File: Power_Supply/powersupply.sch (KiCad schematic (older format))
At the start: 70 parts, among them J101 USB_B_Micro, J2 1x2, J3 1x2, Q1 Q_PMOS_GDS, SW1 KMR2, SW2 joystick-K1-1506DN-01, U1 B0505S-2WR2, U101 AZ1117E-3.3, U102 INA199, U103 ATSAMD10D13A-SS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

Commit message: power supply changes
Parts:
- removed D101: 6V, Diode_SMD:D_SOD-123, symbol Device:D_Zener_Small
- removed R103: 4.99k, Resistor_SMD:R_0805_2012Metric, symbol Device:R_Small_US
- removed U1: B0505S-2WR2, powersupply:B0505S-2WR2-Isolator, symbol powersupply:RFM-0505S
- removed U103: ATSAMD10D13A-SS, Package_SO:SOIC-20W_7.5x12.8mm_P1.27mm, symbol powersupply:ATSAMD10D13A-SS
- added C106: 15uF, Capacitor_SMD:C_0805_2012Metric, symbol Device:C_Small
- added C107: .1 uF, Capacitor_SMD:C_0805_2012Metric, symbol Device:C_Small
- added C108, C109: 15pF, Capacitor_SMD:C_0805_2012Metric, symbol Device:C_Small
- added C110, C111, C112, C113: .1uF, Capacitor_SMD:C_0805_2012Metric, symbol Device:C_Small
- added C114: 1uF, Capacitor_SMD:C_0805_2012Metric, symbol Device:C_Small
- added C115: 10uF, Capacitor_SMD:C_0805_2012Metric, symbol Device:C_Small
- added FB101: ind, Capacitor_SMD:C_0805_2012Metric, symbol Device:Ferrite_Bead_Small
- added R121: 10k, Resistor_SMD:R_0805_2012Metric, symbol Device:R_Small_US
- added Y101: 8MHz, Crystal:Crystal_SMD_5032-2Pin_5.0x3.2mm, symbol Device:Crystal_Small
- Q1: value Q_PMOS_GDS -> IRF9Z24NPBF
- R101: value 150 -> 1k; footprint Resistor_SMD:R_1206_3216Metric -> Resistor_SMD:R_0805_2012Metric
- R111: value 4.99k -> 3.6k
- R116: value 2.32k -> 5.76k
- R120: renamed from R?; value 4.99k -> 1.5k
- R122: renamed from R1; footprint Resistor_THT:R_Axial_DIN0411_L9.9mm_D3.6mm_P12.70mm_Horizontal -> Resistor_SMD:R_0805_2012Metric
- R2: value 580 -> 4.99k
- U103: renamed from U?; value STM32F103C8Tx -> STM32F103C8T6; symbol MCU_ST_STM32F1:STM32F103C8Tx -> powersupply-rescue:STM32F103C8Tx-MCU_ST_STM32F1
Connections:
- net labels removed: SCL, SWCLK, SWDIO
- wire segments 101 -> 129
- no-connect marks 5 -> 17
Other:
- note removed: "2W Isolator"
- moved on the sheet: C103, C104, R104, R105, R111, R112, R120, SW1

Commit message: pin headers
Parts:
- added J4: Conn_01x03_Male, Connector:FanPinHeader_1x03_P2.54mm_Vertical, symbol Connector:Conn_01x03_Male
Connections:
- net GND: now also J4.2 (Pin_2)
- net SWDIO: now reaches U103.34 (PA13)
- net SWDIO: now also J4.1 (Pin_1)
- net SWCLK: now reaches U103.37 (PA14)
- net SWCLK: now also J4.3 (Pin_3)
- no-connect marks 17 -> 15
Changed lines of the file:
@@
 EESchema Schematic File Version 4
 LIBS:powersupply-cache
-EELAYER 29 0
+EELAYER 30 0
 EELAYER END
 $Descr A4 11693 8268
@@
 NoConn ~ 2150 4800
 NoConn ~ 2150 4900
-NoConn ~ 2150 5200
-NoConn ~ 2150 5300
 NoConn ~ 2150 5400
 Wire Notes Line
@@
 $EndComp
 Connection ~ 1050 1650
+$Comp
+L Connector:Conn_01x03_Male J4
+U 1 1 5D9C1B22
+P 2700 5650
+F 0 "J4" H 2808 5931 50  0000 C CNN
+F 1 "Conn_01x03_Male" H 2808 5840 50  0000 C CNN
+F 2 "Connector:FanPinHeader_1x03_P2.54mm_Vertical" H 2700 5650 50  0001 C CNN
+F 3 "~" H 2700 5650 50  0001 C CNN
+	1    2700 5650
+	1    0    0    -1
+$EndComp
+$Comp
+L power:GND #PWR0140
+U 1 1 5D9C2B47
+P 3350 5650
+F 0 "#PWR0140" H 3350 5400 50  0001 C CNN
+F 1 "GND" H 3355 5477 50  0000 C CNN
+F 2 "" H 3350 5650 50  0001 C CNN
+F 3 "" H 3350 5650 50  0001 C CNN
+	1    3350 5650
+	1    0    0    -1
+$EndComp
+Wire Wire Line
+	2900 5650 3350 5650
+Text Label 2900 5550 0    50   ~ 0
+SWDIO
+Text Label 2900 5750 0    50   ~ 0
+SWCLK
+Text Label 2150 5200 0    50   ~ 0
+SWDIO
+Text Label 2150 5300 0    50   ~ 0
+SWCLK
 $EndSCHEMATC

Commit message: save problems
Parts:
- J4: footprint Connector:FanPinHeader_1x03_P2.54mm_Vertical -> Connector_PinSocket_2.54mm:PinSocket_1x03_P2.54mm_Vertical
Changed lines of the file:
@@
 F 0 "J4" H 2808 5931 50  0000 C CNN
 F 1 "Conn_01x03_Male" H 2808 5840 50  0000 C CNN
-F 2 "Connector:FanPinHeader_1x03_P2.54mm_Vertical" H 2700 5650 50  0001 C CNN
+F 2 "Connector_PinSocket_2.54mm:PinSocket_1x03_P2.54mm_Vertical" H 2700 5650 50  0001 C CNN
 F 3 "~" H 2700 5650 50  0001 C CNN
 	1    2700 5650

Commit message: layout changes
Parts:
- D102: renamed from D1; footprint LED_THT:LED_D3.0mm -> LED_SMD:LED_0603_1608Metric_Pad1.05x0.95mm_HandSolder
- R123: renamed from R2; footprint Resistor_THT:R_Axial_DIN0207_L6.3mm_D2.5mm_P10.16mm_Horizontal -> Resistor_SMD:R_0805_2012Metric
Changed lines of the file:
@@
 EESchema Schematic File Version 4
 LIBS:powersupply-cache
-EELAYER 30 0
+EELAYER 29 0
 EELAYER END
 $Descr A4 11693 8268
@@
 	10850 4950 10850 5300
 $Comp
-L Device:LED D1
+L Device:LED D102
 U 1 1 5D62BB53
 P 3950 1300
-F 0 "D1" V 3989 1182 50  0000 R CNN
+F 0 "D102" V 3989 1182 50  0000 R CNN
 F 1 "C503B 2.1V" V 3898 1182 50  0000 R CNN
-F 2 "LED_THT:LED_D3.0mm" H 3950 1300 50  0001 C CNN
+F 2 "LED_SMD:LED_0603_1608Metric_Pad1.05x0.95mm_HandSolder" H 3950 1300 50  0001 C CNN
 F 3 "~" H 3950 1300 50  0001 C CNN
 	1    3950 1300
@@
 	9700 4250 9900 4250
 $Comp
-L Device:R_Small_US R2
+L Device:R_Small_US R123
 U 1 1 5D62CB9E
 P 3950 1050
-F 0 "R2" H 4018 1096 50  0000 L CNN
+F 0 "R123" H 4018 1096 50  0000 L CNN
 F 1 "4.99k" H 4018 1005 50  0000 L CNN
-F 2 "Resistor_THT:R_Axial_DIN0207_L6.3mm_D2.5mm_P10.16mm_Horizontal" H 3950 1050 50  0001 C CNN
+F 2 "Resistor_SMD:R_0805_2012Metric" H 3950 1050 50  0001 C CNN
 F 3 "~" H 3950 1050 50  0001 C CNN
 	1    3950 1050

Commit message: layout
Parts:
- removed TP10: pad_2, powersupply:pads, symbol Connector:TestPoint
- removed TP12: Pad1_default, powersupply:pads, symbol Connector:TestPoint
- removed TP13: pin_2_pad_alt, powersupply:pads, symbol Connector:TestPoint
- removed TP9: pad_1, powersupply:pads, symbol Connector:TestPoint
- added J103, J104: Default_Jumper, powersupply:Default_Jumper, symbol powersupply:Default_Jumper
- D101: renamed from D102; footprint LED_SMD:LED_0603_1608Metric_Pad1.05x0.95mm_HandSolder -> LED_SMD:LED_0805_2012Metric
- FB101: footprint Capacitor_SMD:C_0805_2012Metric -> Capacitor_SMD:C_0805_2012Metric_Pad1.15x1.40mm_HandSolder
- renumbered J3 to J1, J4 to J102
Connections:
- net +3V3: now also J103.1 (A), J104.3 (B); no longer MOD1.2 (VCC)
- net GND: now also J103.3 (B), J104.1 (A); no longer MOD1.1 (GND)
- new net: J104.2 (C), MOD1.1 (GND)
- new net: J103.2 (C), MOD1.2 (VCC)
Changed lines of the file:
@@
 SCK
 $Comp
-L Connector_Generic:Conn_01x02 J3
+L Connector_Generic:Conn_01x02 J1
 U 1 1 5D4A34EF
 P 10650 4850
-F 0 "J3" H 10600 4500 50  0000 L CNN
+F 0 "J1" H 10600 4500 50  0000 L CNN
 F 1 "1x2" H 10600 4600 50  0000 L CNN
 F 2 "powersupply:Banana Sockets" H 10650 5000 50  0001 C CNN
@@
 	10850 4950 10850 5300
 $Comp
-L Device:LED D102
+L Device:LED D101
 U 1 1 5D62BB53
 P 3950 1300
-F 0 "D102" V 3989 1182 50  0000 R CNN
+F 0 "D101" V 3989 1182 50  0000 R CNN
 F 1 "C503B 2.1V" V 3898 1182 50  0000 R CNN
-F 2 "LED_SMD:LED_0603_1608Metric_Pad1.05x0.95mm_HandSolder" H 3950 1300 50  0001 C CNN
+F 2 "LED_SMD:LED_0805_2012Metric" H 3950 1300 50  0001 C CNN
 F 3 "~" H 3950 1300 50  0001 C CNN
 	1    3950 1300
@@
 Wire Wire Line
 	10000 1150 10000 750
-$Comp
-L Connector:TestPoint TP13
-U 1 1 5D5A2114
-P 4400 4000
-F 0 "TP13" H 4342 4026 50  0001 R CNN
-F 1 "pin_2_pad_alt" H 4342 4117 50  0001 R CNN
-F 2 "powersupply:pads" H 4600 4000 50  0001 C CNN
-F 3 "~" H 4600 4000 50  0001 C CNN
-	1    4400 4000
-	-1   0    0    1
-$EndComp
-$Comp
-L Connector:TestPoint TP12
-U 1 1 5D59450B
-P 4400 3600
-F 0 "TP12" H 4458 3718 50  0001 L CNN
-F 1 "Pad1_default" H 4150 3850 50  0001 L CNN
-F 2 "powersupply:pads" H 4600 3600 50  0001 C CNN
-F 3 "~" H 4600 3600 50  0001 C CNN
-	1    4400 3600
-	1    0    0    -1
-$EndComp
-Connection ~ 4400 3600
-$Comp
-L power:GND #PWR06
-U 1 1 5D56D783
-P 4400 3600
-F 0 "#PWR06" H 4400 3350 50  0001 C CNN
-F 1 "GND" H 4250 3500 50  0000 C CNN
-F 2 "" H 4400 3600 50  0001 C CNN
-F 3 "" H 4400 3600 50  0001 C CNN
-	1    4400 3600
-	1    0    0    -1
-$EndComp
-Wire Wire Line
-	4650 3600 4400 3600
 Wire Wire Line
 	4700 3600 4650 3600
-Connection ~ 4650 3600
-$Comp
-L Connector:TestPoint TP9
-U 1 1 5D59F280
-P 4650 3600
-F 0 "TP9" H 4708 3718 50  0001 L CNN
-F 1 "pad_1" H 4450 3550 50  0000 L CNN
-F 2 "powersupply:pads" H 4850 3600 50  0001 C CNN
-F 3 "~" H 4850 3600 50  0001 C CNN
-	1    4650 3600
-	1    0    0    -1
-$EndComp
-Wire Wire Line
-	4650 4000 4400 4000
 Wire Wire Line
 	4700 4000 4650 4000
-Connection ~ 4650 4000
-$Comp
-L Connector:TestPoint TP10
-U 1 1 5D5A6880
-P 4650 4000
-F 0 "TP10" H 4592 4026 50  0001 R CNN
-F 1 "pad_2" H 4850 3950 50  0000 R CNN
-F 2 "powersupply:pads" H 4850 4000 50  0001 C CNN
-F 3 "~" H 4850 4000 50  0001 C CNN
-	1    4650 4000
-	-1   0    0    1
-$EndComp
 $Comp
 L Connector:TestPoint TP11
@@
 F 3 "" H 4950 4400 50  0001 C CNN
 	1    4950 4400
-	1    0    0    -1
-$EndComp
-Connection ~ 4400 4000
-$Comp
-L power:+3.3V #PWR07
-U 1 1 5D56EC9F
-P 4400 4000
-F 0 "#PWR07" H 4400 3850 50  0001 C CNN
-F 1 "+3.3V" H 4250 4050 50  0000 C CNN
-F 2 "" H 4400 4000 50  0001 C CNN
-F 3 "" H 4400 4000 50  0001 C CNN
-	1    4400 4000
 	1    0    0    -1
 $EndComp
@@
 F 0 "FB101" V 1750 2700 50  0000 C CNN
 F 1 "ind" V 1800 2700 50  0000 C CNN
-F 2 "Capacitor_SMD:C_0805_2012Metric" V 1680 2500 50  0001 C CNN
+F 2 "Capacitor_SMD:C_0805_2012Metric_Pad1.15x1.40mm_HandSolder" V 1680 2500 50  0001 C CNN
 F 3 "~" H 1750 2500 50  0001 C CNN
 	1    1750 2500
@@
 Connection ~ 1050 1650
 $Comp
-L Connector:Conn_01x03_Male J4
+L Connector:Conn_01x03_Male J102
 U 1 1 5D9C1B22
 P 2700 5650
-F 0 "J4" H 2808 5931 50  0000 C CNN
+F 0 "J102" H 2808 5931 50  0000 C CNN
 F 1 "Conn_01x03_Male" H 2808 5840 50  0000 C CNN
 F 2 "Connector_PinSocket_2.54mm:PinSocket_1x03_P2.54mm_Vertical" H 2700 5650 50  0001 C CNN
@@
 Text Label 2150 5300 0    50   ~ 0
 SWCLK
+$Comp
+L powersupply:Default_Jumper J104
+U 1 1 5DA84826
+P 4100 3450
+F 0 "J104" V 4146 3328 50  0000 L CNN
+F 1 "Default_Jumper" V 4055 3328 50  0000 L CNN
+F 2 "powersupply:Default_Jumper" H 4100 3450 50  0001 C CNN
+F 3 "" H 4100 3450 50  0001 C CNN
+	1    4100 3450
+	0    -1   -1   0
+$EndComp
+Wire Wire Line
+	4650 3450 4650 3600
+$Comp
+L powersupply:Default_Jumper J103
+U 1 1 5DA8D41B
+P 4100 4300
+F 0 "J103" V 4054 4178 50  0000 L CNN
+F 1 "Default_Jumper" V 4145 4178 50  0000 L CNN
+F 2 "powersupply:Default_Jumper" H 4100 4300 50  0001 C CNN
+F 3 "" H 4100 4300 50  0001 C CNN
+	1    4100 4300
+	0    -1   1    0
+$EndComp
+Wire Wire Line
+	4650 4000 4650 4300
+$Comp
+L power:GND #PWR0141
+U 1 1 5DA962E0
+P 4400 3750
+F 0 "#PWR0141" H 4400 3500 50  0001 C CNN
+F 1 "GND" H 4550 3650 50  0000 C CNN
+F 2 "" H 4400 3750 50  0001 C CNN
+F 3 "" H 4400 3750 50  0001 C CNN
+	1    4400 3750
+	1    0    0    -1
+$EndComp
+$Comp
+L power:+3.3V #PWR0142
+U 1 1 5DA968DF
+P 4400 4000
+F 0 "#PWR0142" H 4400 3850 50  0001 C CNN
+F 1 "+3.3V" H 4250 4050 50  0000 C CNN
+F 2 "" H 4400 4000 50  0001 C CNN
+F 3 "" H 4400 4000 50  0001 C CNN
+	1    4400 4000
+	1    0    0    -1
+$EndComp
+$Comp
+L power:+3.3V #PWR0143
+U 1 1 5DA975C6
+P 4400 3150
+F 0 "#PWR0143" H 4400 3000 50  0001 C CNN
+F 1 "+3.3V" H 4250 3200 50  0000 C CNN
+F 2 "" H 4400 3150 50  0001 C CNN
+F 3 "" H 4400 3150 50  0001 C CNN
+	1    4400 3150
+	1    0    0    -1
+$EndComp
+$Comp
+L power:GND #PWR0144
+U 1 1 5DA97C54
+P 4400 4600
+F 0 "#PWR0144" H 4400 4350 50  0001 C CNN
+F 1 "GND" H 4550 4500 50  0000 C CNN
+F 2 "" H 4400 4600 50  0001 C CNN
+F 3 "" H 4400 4600 50  0001 C CNN
+	1    4400 4600
+	1    0    0    -1
+$EndComp
 $EndSCHEMATC

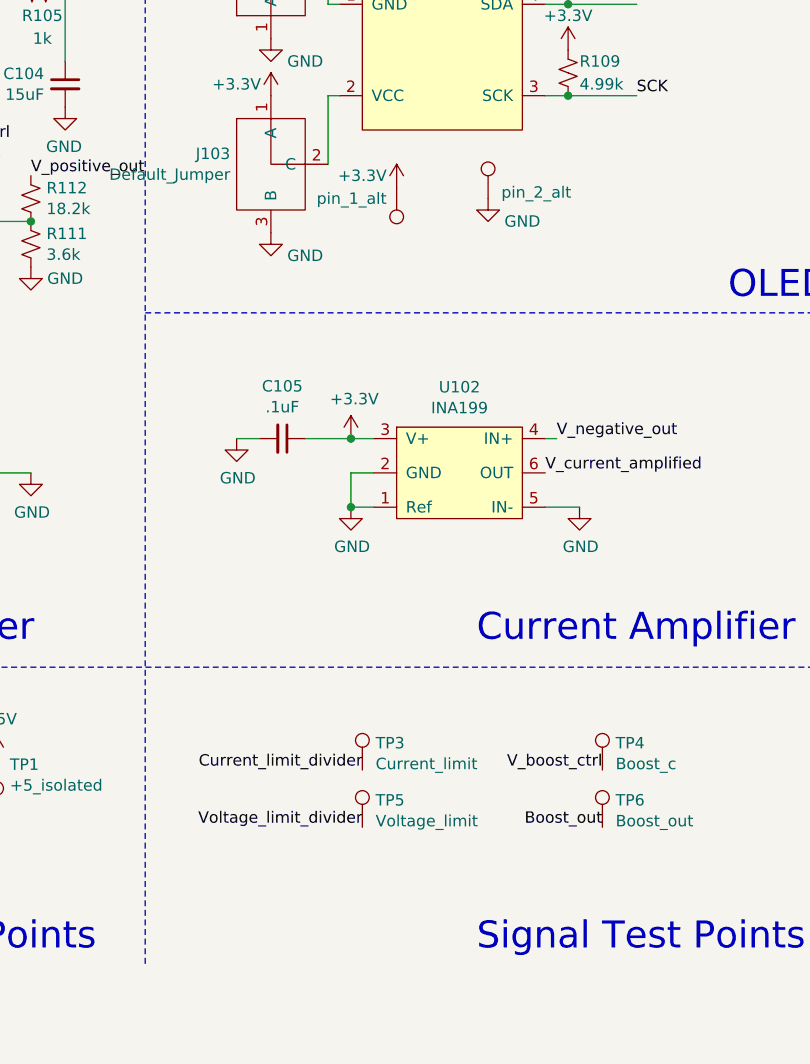
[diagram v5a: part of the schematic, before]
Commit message: Added fiducials for automated assembly
Added fiducials for automated assembly
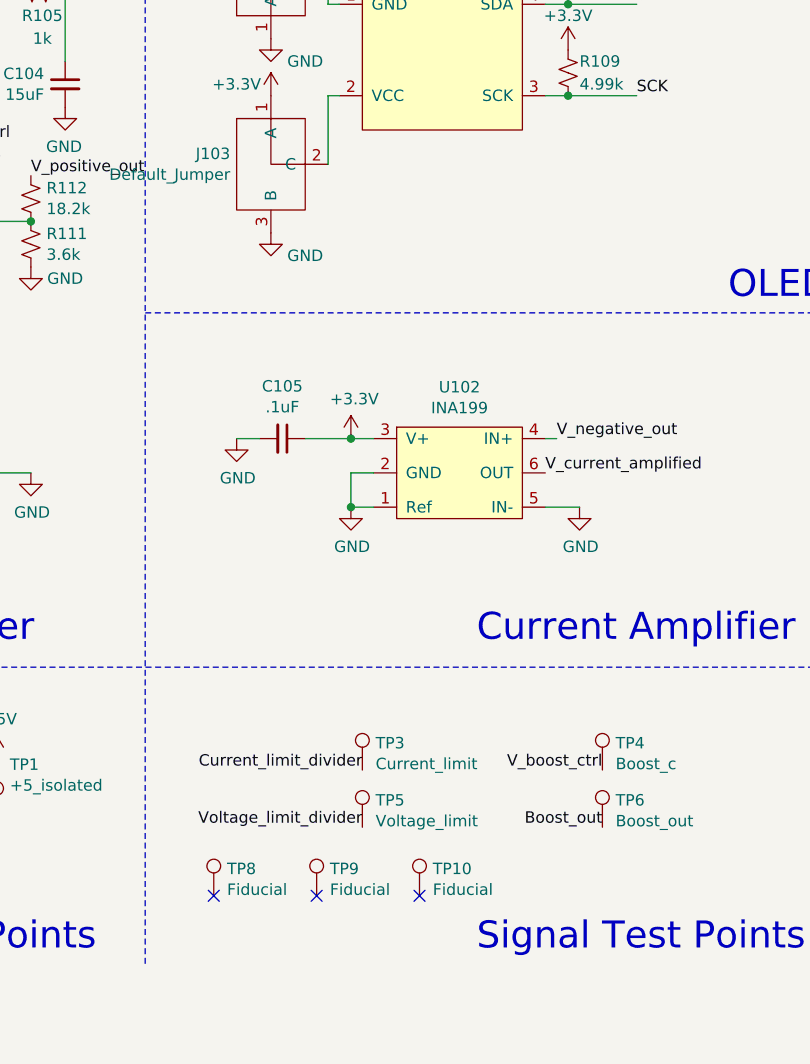
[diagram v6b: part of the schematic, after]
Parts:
- removed TP11: pin_2_alt, powersupply:pads, symbol Connector:TestPoint
- added TP10, TP9: Fiducial, Fiducial:Fiducial_0.75mm_Dia_1.5mm_Outer, symbol Connector:TestPoint
- TP8: value pin_1_alt -> Fiducial; footprint powersupply:pads -> Fiducial:Fiducial_0.75mm_Dia_1.5mm_Outer
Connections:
- net +3V3: no longer TP8.1
- no-connect marks 15 -> 18
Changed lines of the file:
@@
 EESchema Schematic File Version 4
 LIBS:powersupply-cache
-EELAYER 29 0
+EELAYER 26 0
 EELAYER END
 $Descr A4 11693 8268
@@
 $EndComp
 $Comp
-L power:GND #PWR08
-U 1 1 5D56DFE0
-P 5350 4450
-F 0 "#PWR08" H 5350 4200 50  0001 C CNN
-F 1 "GND" H 5500 4350 50  0000 C CNN
-F 2 "" H 5350 4450 50  0001 C CNN
-F 3 "" H 5350 4450 50  0001 C CNN
-	1    5350 4450
-	1    0    0    -1
-$EndComp
-$Comp
-L Connector:TestPoint TP8
-U 1 1 5D58A893
-P 4950 4400
-F 0 "TP8" H 4892 4426 50  0001 R CNN
-F 1 "pin_1_alt" H 5300 4450 50  0000 R CNN
-F 2 "powersupply:pads" H 5150 4400 50  0001 C CNN
-F 3 "~" H 5150 4400 50  0001 C CNN
-	1    4950 4400
-	-1   0    0    1
-$EndComp
-$Comp
 L powersupply:INA199 U102
 U 1 1 5D650116
@@
 Wire Wire Line
 	4700 4000 4650 4000
-$Comp
-L Connector:TestPoint TP11
-U 1 1 5D59533A
-P 5350 4450
-F 0 "TP11" H 5408 4568 50  0001 L CNN
-F 1 "pin_2_alt" H 5408 4477 50  0000 L CNN
-F 2 "powersupply:pads" H 5550 4450 50  0001 C CNN
-F 3 "~" H 5550 4450 50  0001 C CNN
-	1    5350 4450
-	1    0    0    -1
-$EndComp
-$Comp
-L power:+3.3V #PWR05
-U 1 1 5D56E643
-P 4950 4400
-F 0 "#PWR05" H 4950 4250 50  0001 C CNN
-F 1 "+3.3V" H 4800 4450 50  0000 C CNN
-F 2 "" H 4950 4400 50  0001 C CNN
-F 3 "" H 4950 4400 50  0001 C CNN
-	1    4950 4400
-	1    0    0    -1
-$EndComp
 $Comp
 L Device:D_Schottky_Small D2
@@
 	1    0    0    -1
 $EndComp
+$Comp
+L Connector:TestPoint TP8
+U 1 1 5DA56401
+P 4150 7500
+F 0 "TP8" H 4208 7618 50  0000 L CNN
+F 1 "Fiducial" H 4208 7527 50  0000 L CNN
+F 2 "Fiducial:Fiducial_0.75mm_Dia_1.5mm_Outer" H 4350 7500 50  0001 C CNN
+F 3 "~" H 4350 7500 50  0001 C CNN
+	1    4150 7500
+	1    0    0    -1
+$EndComp
+$Comp
+L Connector:TestPoint TP9
+U 1 1 5DA5D582
+P 4600 7500
+F 0 "TP9" H 4658 7618 50  0000 L CNN
+F 1 "Fiducial" H 4658 7527 50  0000 L CNN
+F 2 "Fiducial:Fiducial_0.75mm_Dia_1.5mm_Outer" H 4800 7500 50  0001 C CNN
+F 3 "~" H 4800 7500 50  0001 C CNN
+	1    4600 7500
+	1    0    0    -1
+$EndComp
+$Comp
+L Connector:TestPoint TP10
+U 1 1 5DA5D941
+P 5050 7500
+F 0 "TP10" H 5108 7618 50  0000 L CNN
+F 1 "Fiducial" H 5108 7527 50  0000 L CNN
+F 2 "Fiducial:Fiducial_0.75mm_Dia_1.5mm_Outer" H 5250 7500 50  0001 C CNN
+F 3 "~" H 5250 7500 50  0001 C CNN
+	1    5050 7500
+	1    0    0    -1
+$EndComp
+NoConn ~ 4150 7500
+NoConn ~ 4600 7500
+NoConn ~ 5050 7500
 $EndSCHEMATC

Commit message: bug 1/3
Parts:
- added R?: 1.5k, Resistor_SMD:R_0805_2012Metric, symbol Device:R_Small_US
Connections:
- net +3V3: now also R?.1
- net at U103.20 (PB2): now also R?.2
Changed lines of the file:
@@
 EESchema Schematic File Version 4
 LIBS:powersupply-cache
-EELAYER 26 0
+EELAYER 30 0
 EELAYER END
 $Descr A4 11693 8268
@@
 NoConn ~ 4600 7500
 NoConn ~ 5050 7500
+$Comp
+L Device:R_Small_US R?
+U 1 1 5DC15C01
+P 700 4000
+F 0 "R?" H 600 4100 50  0000 C CNN
+F 1 "1.5k" H 550 4000 50  0000 C CNN
+F 2 "Resistor_SMD:R_0805_2012Metric" H 700 4000 50  0001 C CNN
+F 3 "~" H 700 4000 50  0001 C CNN
+	1    700  4000
+	1    0    0    -1
+$EndComp
+Wire Wire Line
+	700  4100 850  4100
+$Comp
+L power:+3.3V #PWR?
+U 1 1 5DC39F86
+P 700 3900
+F 0 "#PWR?" H 700 3750 50  0001 C CNN
+F 1 "+3.3V" H 715 4073 50  0000 C CNN
+F 2 "" H 700 3900 50  0001 C CNN
+F 3 "" H 700 3900 50  0001 C CNN
+	1    700  3900
+	1    0    0    -1
+$EndComp
 $EndSCHEMATC
